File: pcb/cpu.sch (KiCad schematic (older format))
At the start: 113 parts, among them J1 Conn_02x16_Counter_Clockwise, J2 Conn_01x16, U1 74LS283, U2 74LS283, U3 74LS283, U4 74LS283

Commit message: select memory segment output
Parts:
- removed U? (x2): 74AUC1G18, symbol 74xGxx:74AUC1G18
- added U?: 74AHCT1G04, symbol 74xGxx:74AHCT1G04
- added U? (x2): 74AUC1G18, symbol 74xGxx:74AUC1G18
- added U? (x3): mux16, symbol nand2tetris:mux16
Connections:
- net GND: now also U?.2 (GND), U?.2 (GND), U?.3 (GND)
- net VCC: now also U?.5 (VCC), U?.5 (VCC), U?.5 (VCC)
- net adr13: now also U?.1
- net adr14: now also U?.1
- net lkbd: now also U?.4
- net load: now also U?.3
- net low: now also U?.12 (8B2), U?.12 (8B2), U?.17 (10B2), U?.17 (10B2), U?.20 (12B2), U?.20 (12B2), U?.23 (14B2), U?.23 (14B2), U?.26 (16B2), U?.26 (16B2), U?.3 (2B2), U?.3 (2B2), U?.32 (15B2), U?.32 (15B2), U?.35 (13B2), U?.35 (13B2), U?.38 (11B2), U?.38 (11B2), U?.41 (9B2), U?.41 (9B2), U?.46 (7B2), U?.46 (7B2), U?.49 (5B2), U?.49 (5B2), U?.52 (3B2), U?.52 (3B2), U?.55 (1B2), U?.55 (1B2), U?.6 (4B2), U?.6 (4B2), U?.9 (6B2), U?.9 (6B2), U?.0 (out), U?.1 (out), U?.10 (out), U?.11 (out), U?.12 (out), U?.13 (out), U?.14 (out), U?.15 (out), U?.2 (out), U?.3 (out), U?.4 (out), U?.5 (out), U?.6 (out), U?.7 (out), U?.8 (out), U?.9 (out)
- net lram: now also U?.6
- net lvram: now also U?.6
- net at U?.6 (~CE~): now also U?.4
- new net: U?.3, U?.4
- new net CLK: U?.2
- new net addr13: U?.~ (VCC)
- new net addr14: U?.~ (VCC)
- new net addrow: U?.~ (VCC)
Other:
- note added: "kbd"
- note added: "ram"
- note added: "vram"
- moved on the sheet: U?

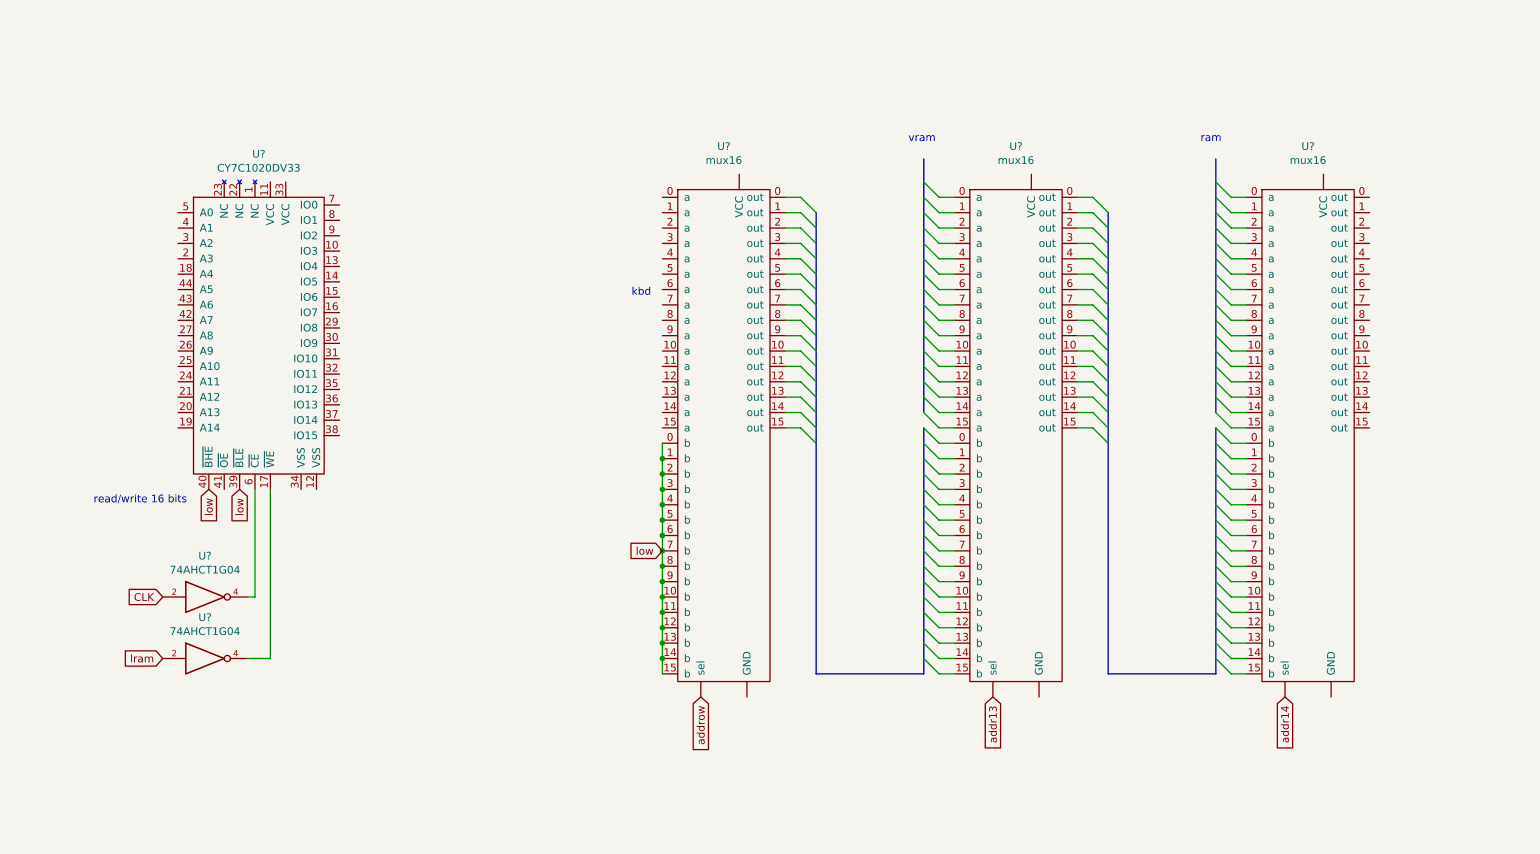
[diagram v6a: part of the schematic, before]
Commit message: memory segment select
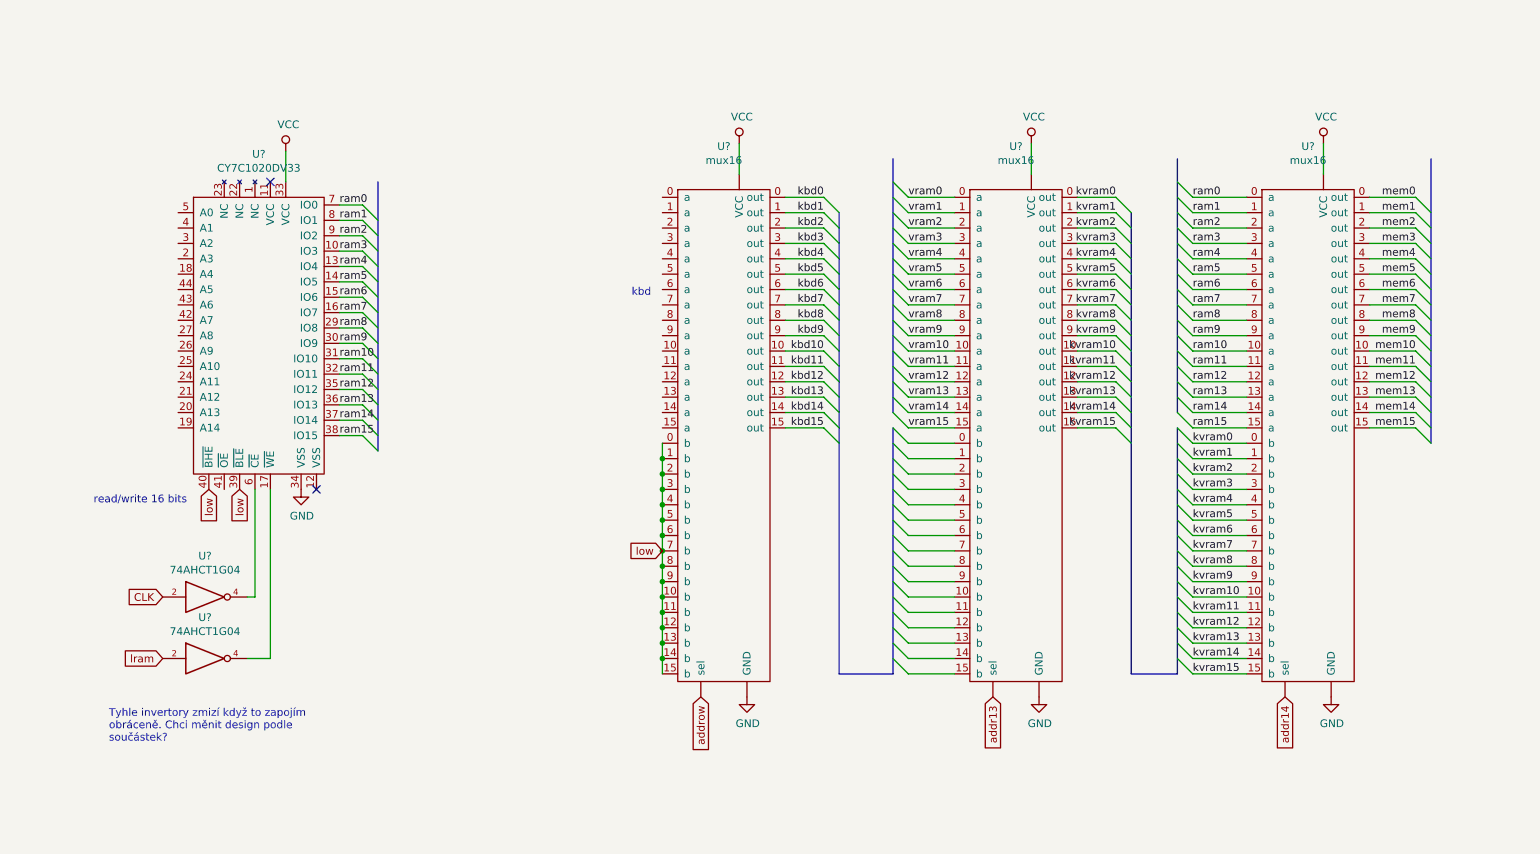
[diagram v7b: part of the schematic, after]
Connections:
- net GND: now also U?.34 (VSS), U?.~ (VCC), U?.~ (VCC), U?.~ (VCC)
- net VCC: now also U?.33 (VCC), U?.~ (VCC), U?.~ (VCC), U?.~ (VCC)
- net ram3: now reaches U?.10 (IO3)
- net ram3: now also U?.3 (out)
- net ram4: now reaches U?.13 (IO4)
- net ram4: now also U?.4 (out)
- net ram5: now reaches U?.14 (IO5)
- net ram5: now also U?.5 (out)
- net ram6: now reaches U?.15 (IO6)
- net ram6: now also U?.6 (out)
- net ram7: now reaches U?.16 (IO7)
- net ram7: now also U?.7 (out)
- net ram8: now reaches U?.29 (IO8)
- net ram8: now also U?.8 (out)
- net ram9: now reaches U?.30 (IO9)
- net ram9: now also U?.9 (out)
- net ram10: now reaches U?.31 (IO10)
- net ram10: now also U?.10 (out)
- net ram11: now reaches U?.32 (IO11)
- net ram11: now also U?.11 (out)
- net ram12: now reaches U?.35 (IO12)
- net ram12: now also U?.12 (out)
- net ram13: now reaches U?.36 (IO13)
- net ram13: now also U?.13 (out)
- net ram14: now reaches U?.37 (IO14)
- net ram14: now also U?.14 (out)
- net ram15: now reaches U?.38 (IO15)
- net ram15: now also U?.15 (out)
- net ram0: now reaches U?.7 (IO0)
- net ram0: now also U?.0 (out)
- net ram1: now reaches U?.8 (IO1)
- net ram1: now also U?.1 (out)
- net ram2: now reaches U?.9 (IO2)
- net ram2: now also U?.2 (out)
- net vram0: now reaches U?.0 (out)
- net vram1: now reaches U?.1 (out)
- net vram10: now reaches U?.10 (out)
- net vram11: now reaches U?.11 (out)
- net vram12: now reaches U?.12 (out)
- net vram13: now reaches U?.13 (out)
- net vram14: now reaches U?.14 (out)
- net vram15: now reaches U?.15 (out)
- net vram2: now reaches U?.2 (out)
- net vram3: now reaches U?.3 (out)
- net vram4: now reaches U?.4 (out)
- net vram5: now reaches U?.5 (out)
- net vram6: now reaches U?.6 (out)
- net vram7: now reaches U?.7 (out)
- net vram8: now reaches U?.8 (out)
- net vram9: now reaches U?.9 (out)
- new net kbd0: U?.0 (out)
- new net kbd1: U?.1 (out)
- new net kbd10: U?.10 (out)
- new net kbd11: U?.11 (out)
- new net kbd12: U?.12 (out)
- new net kbd13: U?.13 (out)
- new net kbd14: U?.14 (out)
- new net kbd15: U?.15 (out)
- new net kbd2: U?.2 (out)
- new net kbd3: U?.3 (out)
- new net kbd4: U?.4 (out)
- new net kbd5: U?.5 (out)
- new net kbd6: U?.6 (out)
- new net kbd7: U?.7 (out)
- new net kbd8: U?.8 (out)
- new net kbd9: U?.9 (out)
- new net kvram0: U?.0 (out), U?.0 (out)
- new net kvram1: U?.1 (out), U?.1 (out)
- new net kvram10: U?.10 (out), U?.10 (out)
- new net kvram11: U?.11 (out), U?.11 (out)
- new net kvram12: U?.12 (out), U?.12 (out)
- new net kvram13: U?.13 (out), U?.13 (out)
- new net kvram14: U?.14 (out), U?.14 (out)
- new net kvram15: U?.15 (out), U?.15 (out)
- new net kvram2: U?.2 (out), U?.2 (out)
- new net kvram3: U?.3 (out), U?.3 (out)
- new net kvram4: U?.4 (out), U?.4 (out)
- new net kvram5: U?.5 (out), U?.5 (out)
- new net kvram6: U?.6 (out), U?.6 (out)
- new net kvram7: U?.7 (out), U?.7 (out)
- new net kvram8: U?.8 (out), U?.8 (out)
- new net kvram9: U?.9 (out), U?.9 (out)
- new net mem0: U?.0 (out)
- new net mem1: U?.1 (out)
- new net mem10: U?.10 (out)
- new net mem11: U?.11 (out)
- new net mem12: U?.12 (out)
- new net mem13: U?.13 (out)
- new net mem14: U?.14 (out)
- new net mem15: U?.15 (out)
- new net mem2: U?.2 (out)
- new net mem3: U?.3 (out)
- new net mem4: U?.4 (out)
- new net mem5: U?.5 (out)
- new net mem6: U?.6 (out)
- new net mem7: U?.7 (out)
- new net mem8: U?.8 (out)
- new net mem9: U?.9 (out)
- no-connect marks 37 -> 39
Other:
- note added: "Tyhle invertory zmizí když to zapojím\nobráceně. Chci měnit design podle\nsoučástek?"
- note removed: "ram"
- note removed: "vram"

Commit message: memory
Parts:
- added U? (x14): 74LVC2G32, symbol 74xGxx:74LVC2G32
- added U?: 74FCT163374APAG8, symbol nand2tetris:74FCT163374APAG8
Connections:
- net labels added: addr0, addr1, addr10, addr11, addr12, addr2, addr3, addr4, addr5, addr6, addr7, addr8, addr9
- net labels removed: addrow
- wire segments 530 -> 612
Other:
- note added: "výběr segmentu paměti"
- note added: "výpočet překročení maximální\npaměti - 0x6000"
- note removed: "kbd"
- moved on the sheet: U?
